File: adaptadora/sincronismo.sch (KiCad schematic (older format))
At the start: 60 parts

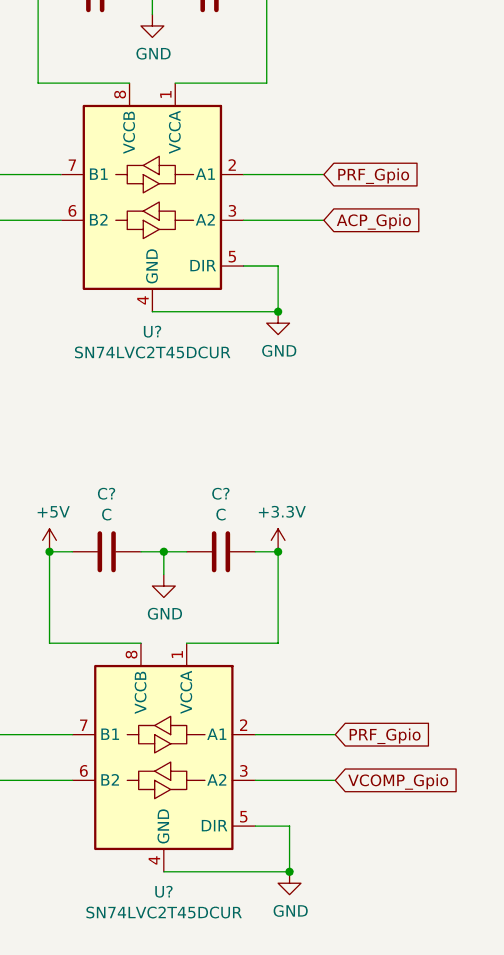
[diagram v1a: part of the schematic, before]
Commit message: esquemático terminado faltan valores
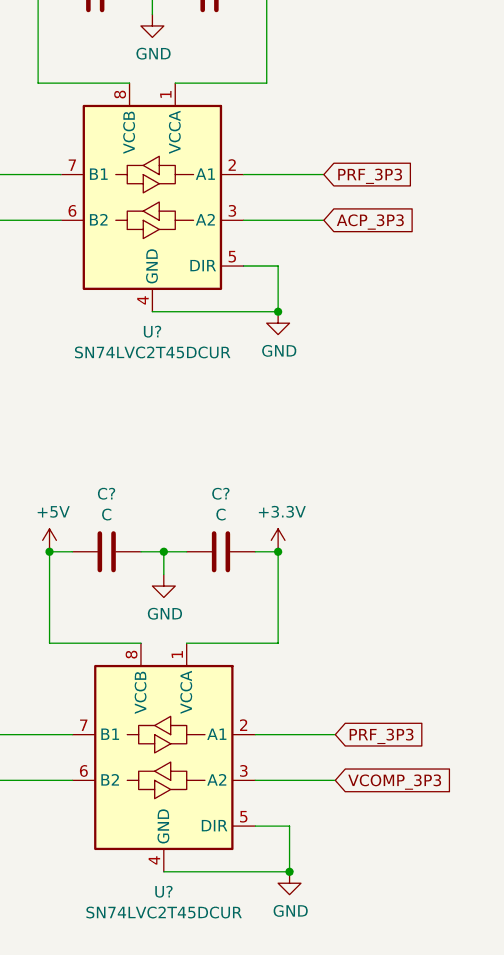
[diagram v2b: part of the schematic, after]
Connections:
- net ACP_Gpio renamed ACP_3P3
- net PRF_Gpio renamed PRF_3P3
- net VCOMP_Gpio renamed VCOMP_3P3
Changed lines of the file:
@@
 $EndComp
 Text GLabel 10650 2500 2    50   Input ~ 0
-ACP_Gpio
+ACP_3P3
 Text GLabel 10650 2300 2    50   Input ~ 0
-PRF_Gpio
+PRF_3P3
 $Comp
 L Logic_LevelTranslator:SN74LVC2T45DCUR U?
@@
 $EndComp
 Text GLabel 10700 4950 2    50   Input ~ 0
-VCOMP_Gpio
+VCOMP_3P3
 Text GLabel 10700 4750 2    50   Input ~ 0
-PRF_Gpio
+PRF_3P3
 $Comp
 L Logic_LevelTranslator:SN74LVC2T45DCUR U?

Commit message: se enumeraron componentes faltan valores
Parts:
- gave numbers to parts that had none: 60

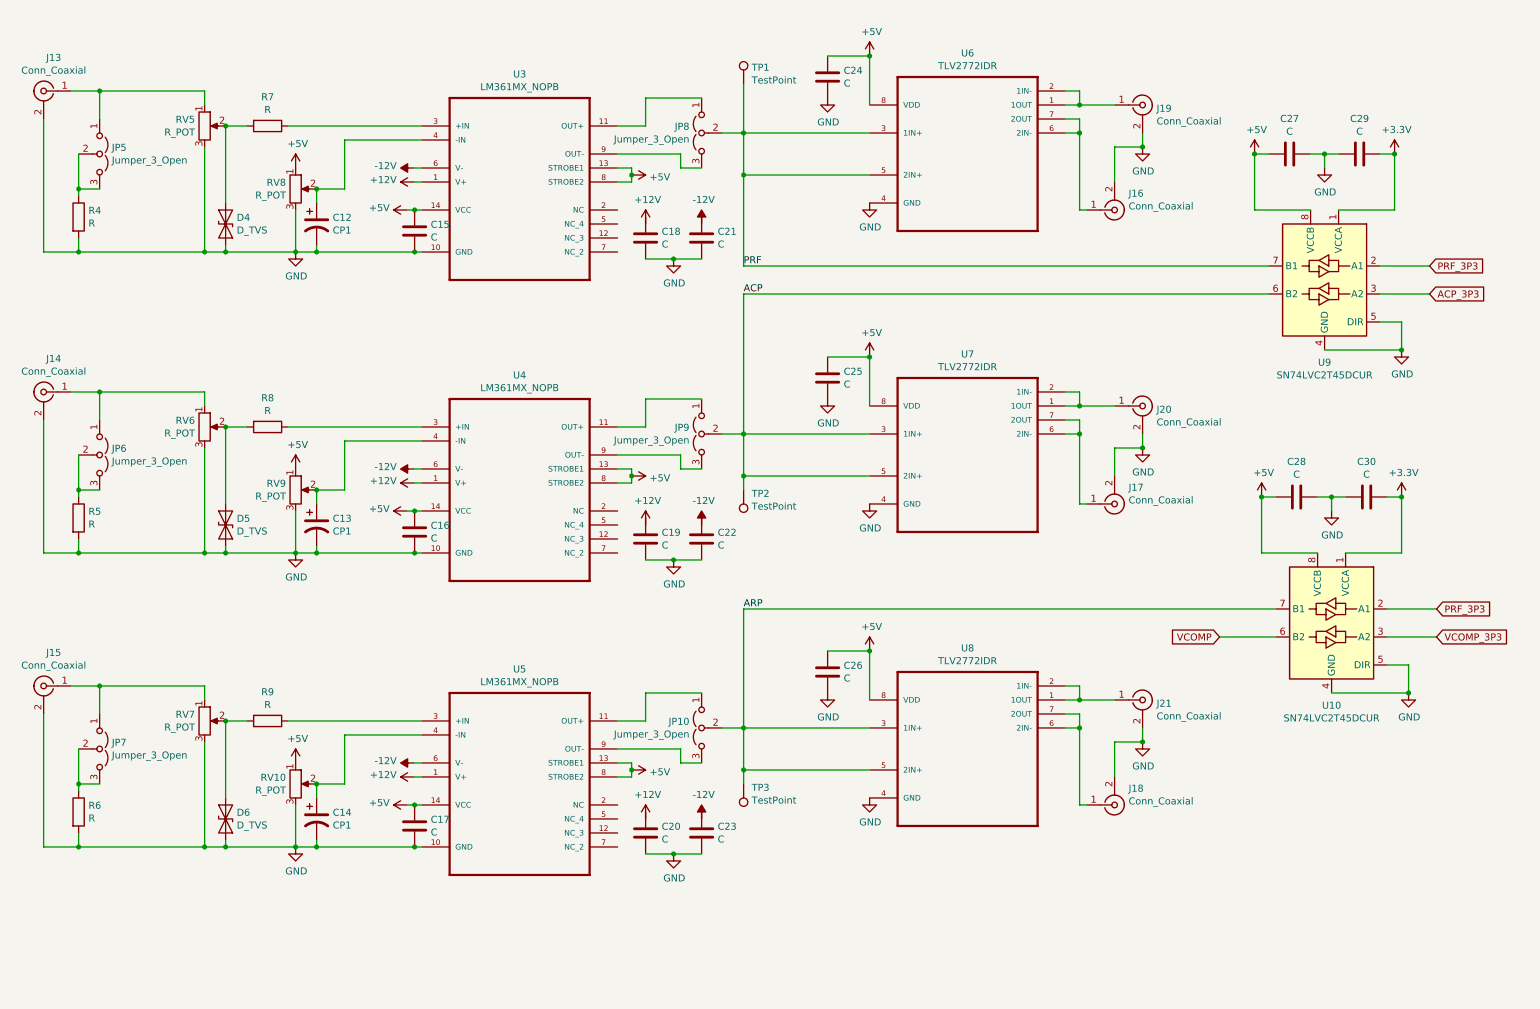
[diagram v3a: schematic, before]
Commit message: se agregan valores, etiquetas jerarquicas y poligonos
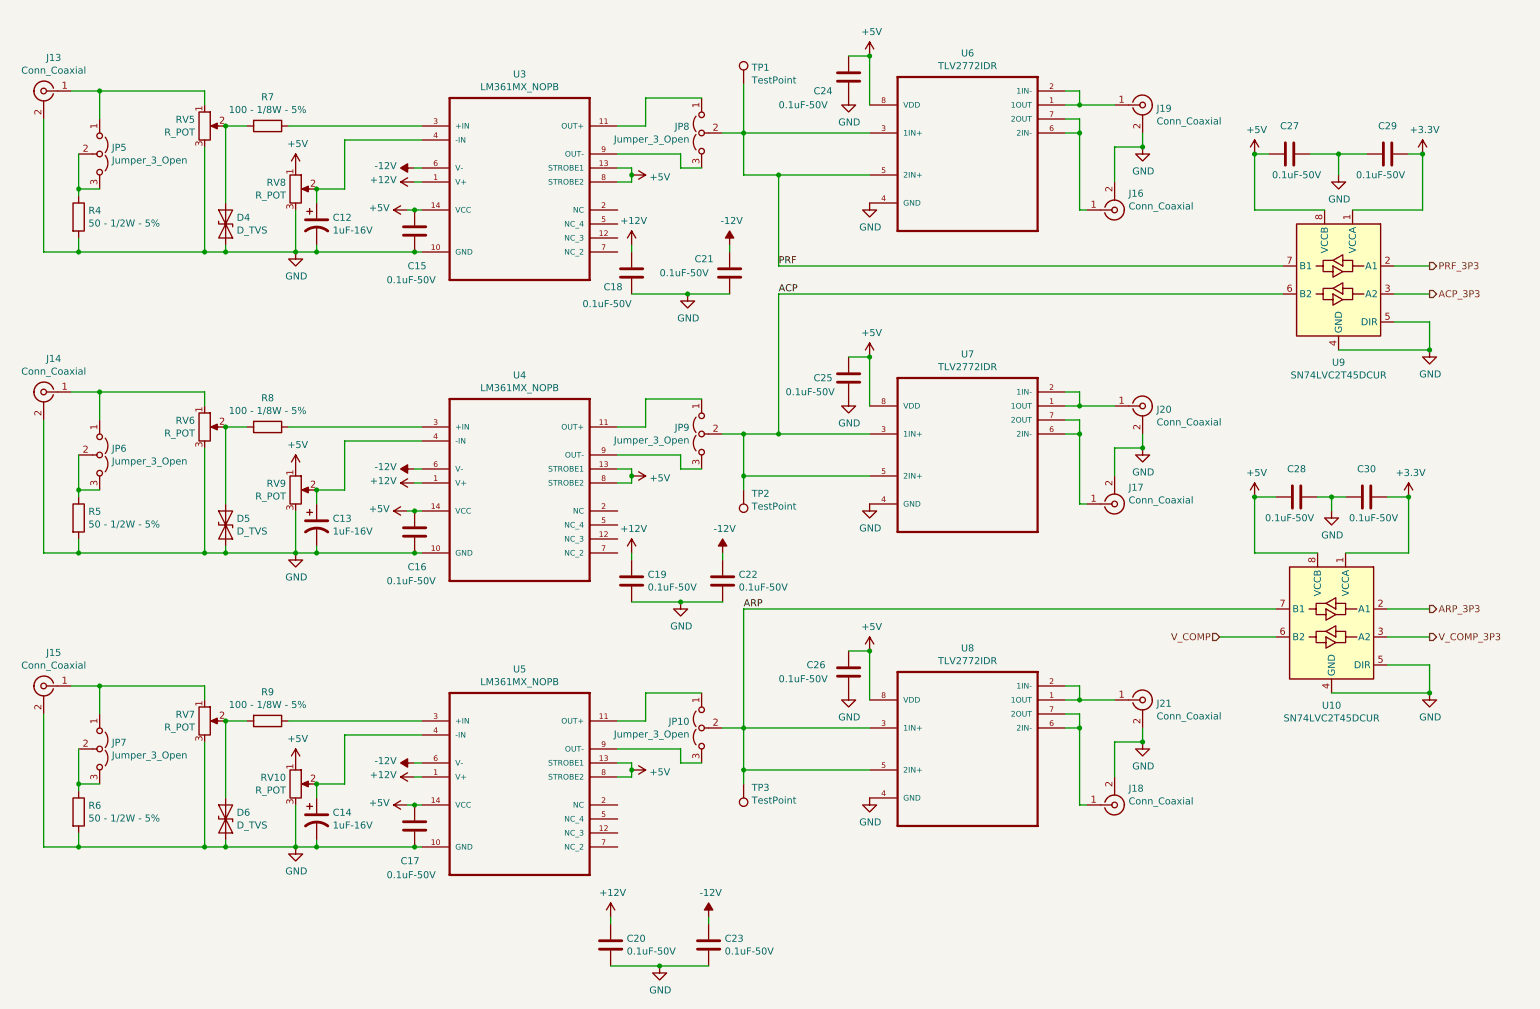
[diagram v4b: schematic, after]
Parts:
- C12, C13, C14: value CP1 -> 1uF-16V
- C15, C16, C17, C18, C19, C20, C21, C22, C23, C24, C25, C26, C27, C28, C29, C30: value C -> 0.1uF-50V
- R4, R5, R6: value R -> 50 - 1/2W - 5%
- R7, R8, R9: value R -> 100 - 1/8W - 5%
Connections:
- net +12V: now also C18.1, C19.1, C20.1
- net -12V: now also C21.1, C22.1, C23.1
- net PRF_3P3: no longer U10.2 (A1)
- net VCOMP renamed V_COMP
- net VCOMP_3P3 renamed V_COMP_3P3
- new net ARP_3P3: U10.2 (A1)
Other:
- moved on the sheet: C18, C19, C20, C21, C22, C23, C24, C25, C26, C29, U9

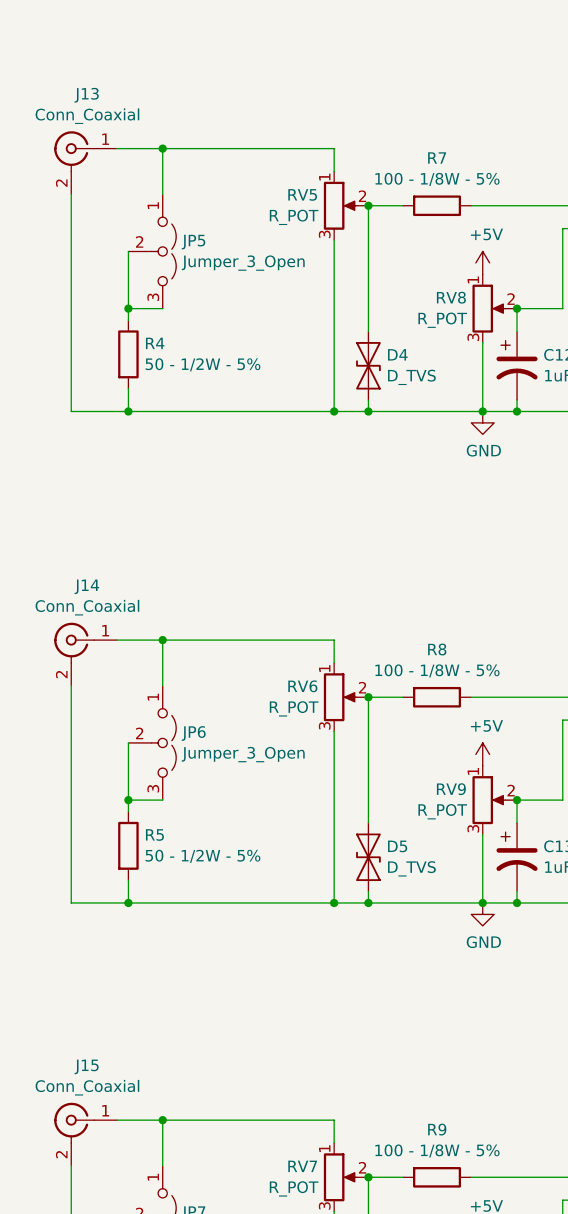
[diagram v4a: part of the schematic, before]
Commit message: se agrega texto
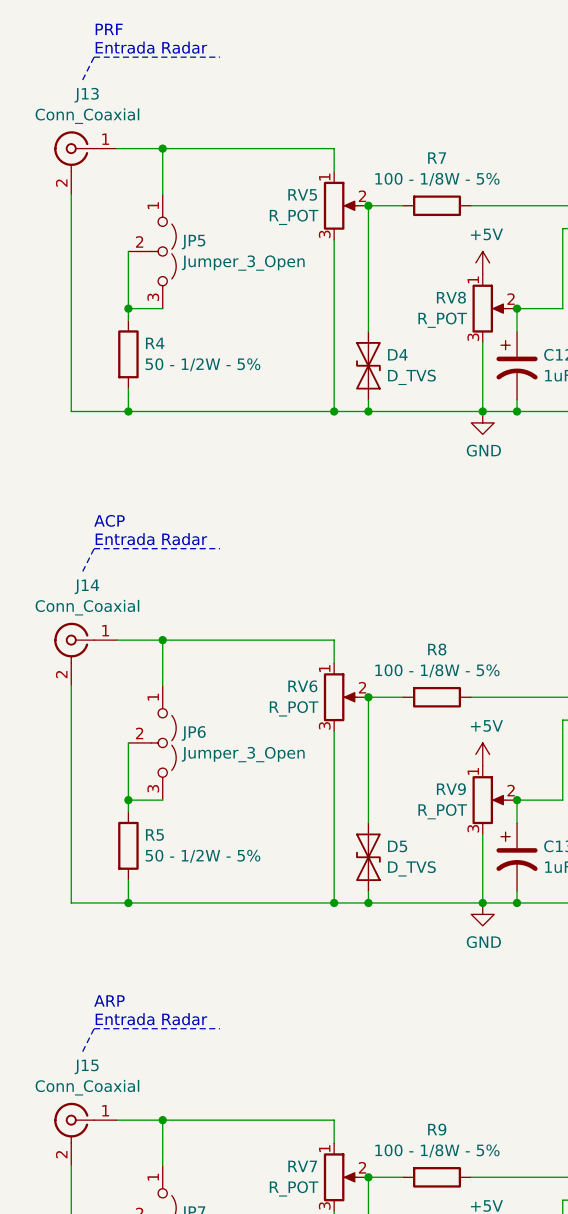
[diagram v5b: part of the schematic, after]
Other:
- note added: "ACP\nEntrada Radar"
- note added: "ARP\nEntrada Radar"
- note added: "PRF\nEntrada Radar"
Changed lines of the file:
@@
 	10350 5150 10650 5150
 Connection ~ 10650 5350
+Wire Notes Line
+	800  750  850  650
+Text Notes 850  650  0    50   ~ 0
+PRF\nEntrada Radar
+Wire Notes Line
+	850  650  1400 650
+Wire Notes Line
+	800  2900 850  2800
+Text Notes 850  2800 0    50   ~ 0
+ACP\nEntrada Radar
+Wire Notes Line
+	850  2800 1400 2800
+Wire Notes Line
+	800  5000 850  4900
+Text Notes 850  4900 0    50   ~ 0
+ARP\nEntrada Radar
+Wire Notes Line
+	850  4900 1400 4900
 $EndSCHEMATC
